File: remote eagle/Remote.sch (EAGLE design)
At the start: 17 parts, among them IC1 ATmega328p, J1 ISP Touch, Y1 16MHz, Y2 ANTENNA2ANTENNA-CHIP_1204

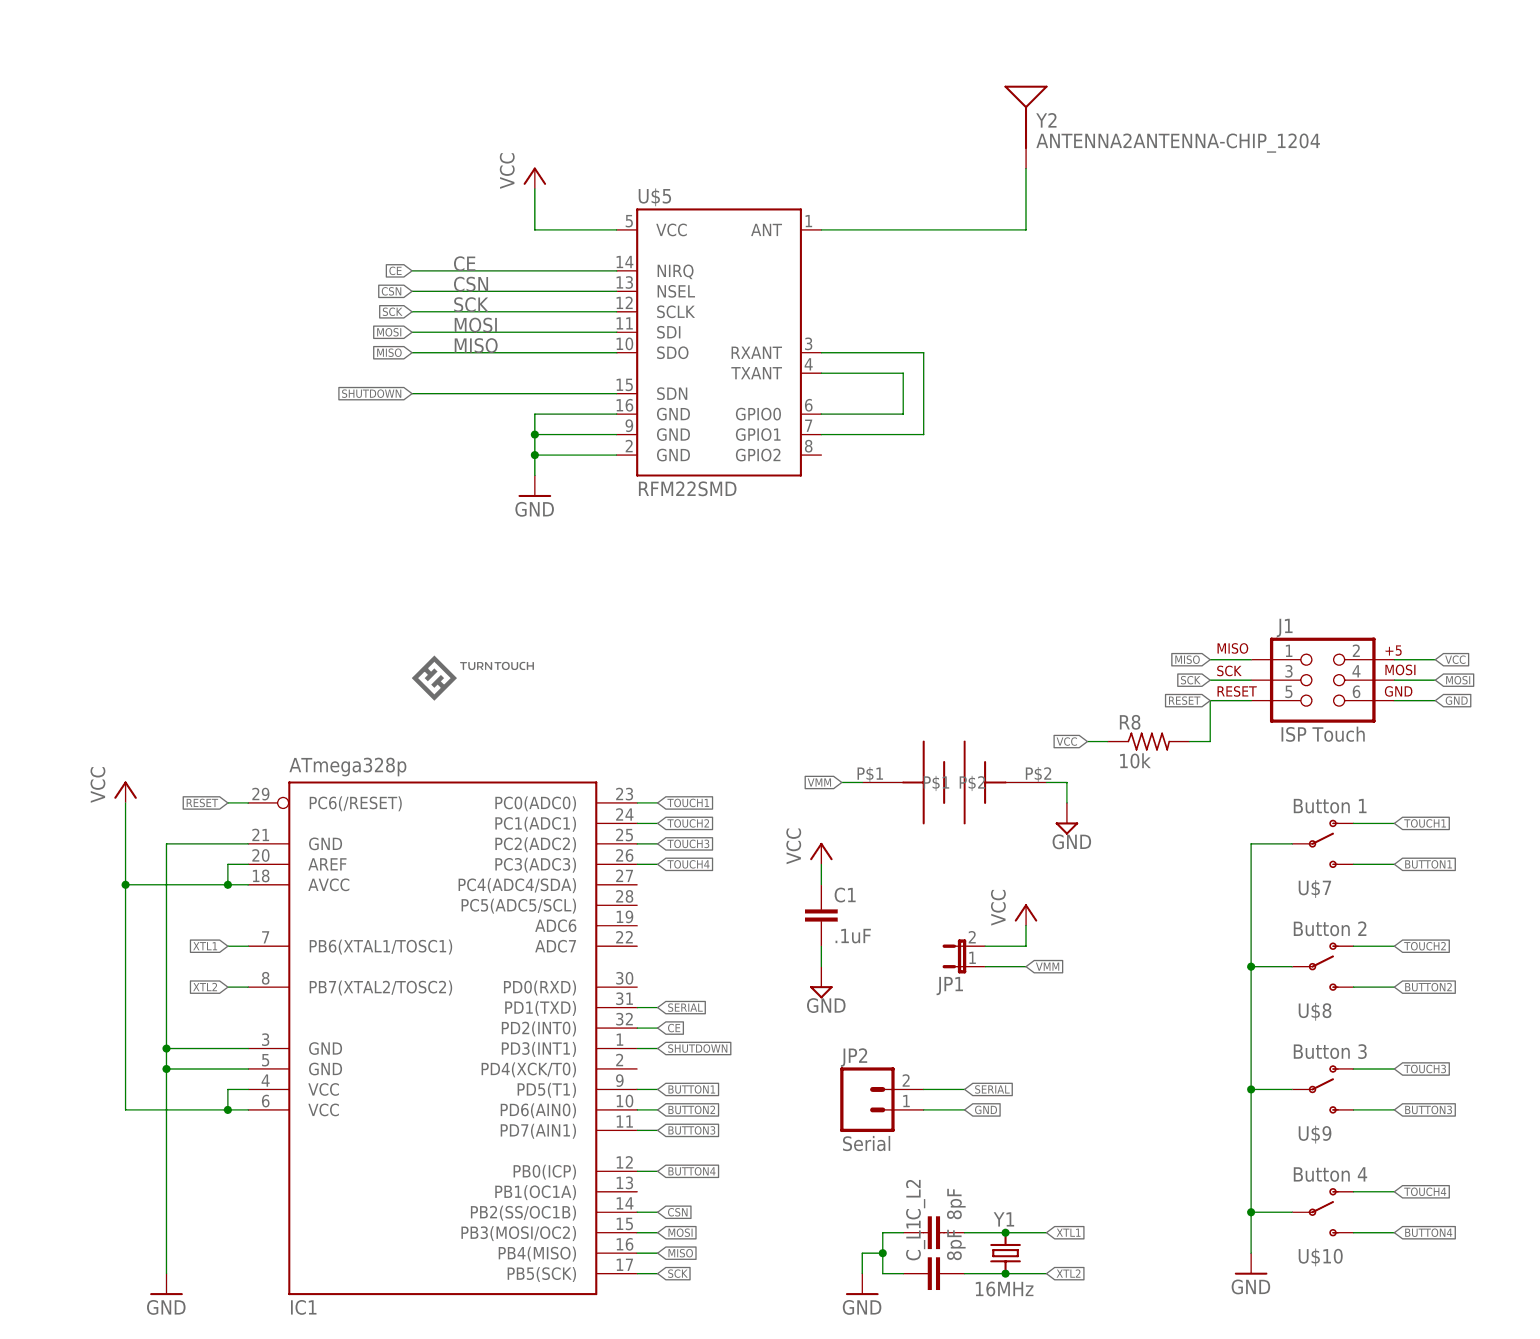
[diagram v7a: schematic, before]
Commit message: Switching to BLE112 and new P-Series dome by Snaptron in schematic and board.
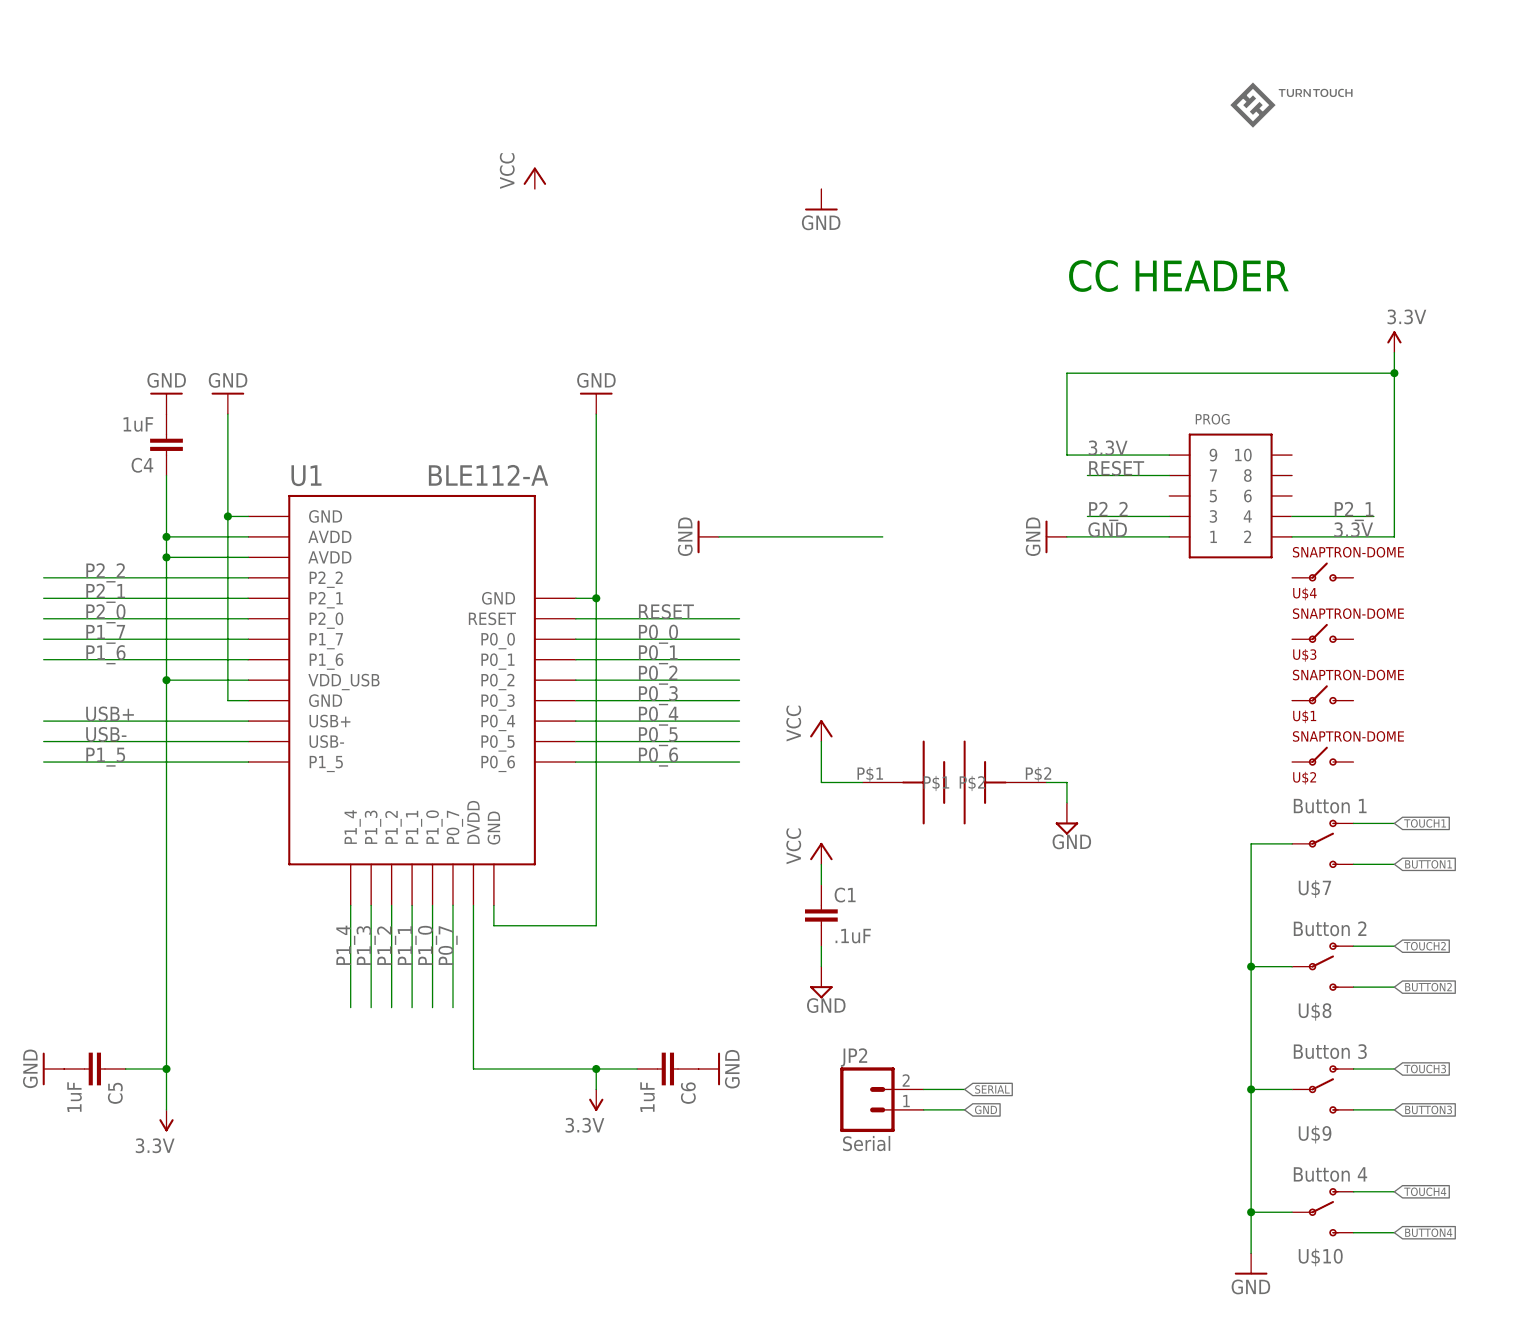
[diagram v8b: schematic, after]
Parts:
- removed C_L1, C_L2: 8pF, SparkFun-Passives:CAP0402-CAP
- removed IC1: ATmega328p, atmel:MEGA8-MI
- removed J1: ISP Touch, remote:ISPTOUCH_HEADER
- removed JP1: (no value), SparkFun-Passives:JUMPER-2SMD-NC
- removed R8: 10k, resistor:R-US_R0402
- removed U$5: RFM22SMD, remote:RFM22SMD
- removed Y1: 16MHz, remote:CRYSTAL5X3.2
- removed Y2: ANTENNA2ANTENNA-CHIP_1204, remote:ANTENNA2ANTENNA-CHIP_1204
- added C4, C5, C6: 1uF, SparkFun:CAP0603-CAP
- added PROG: CONN_5-2-FTSH-V, pel_misc:CONN_5-2-FTSH-V
- added U$1, U$2, U$3, U$4: SNAPTRON-DOME, remote:SNAPTRON-DOME
- added U1: BLE112-A, sf-bluegiga:BLE112-A-VISUAL
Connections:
- removed net CE: IC1.PD2(INT0), U$5.NIRQ
- removed net CSN: IC1.PB2(SS/OC1B), U$5.NSEL
- removed net MISO: IC1.PB4(MISO), J1.1, U$5.SDO
- removed net MOSI: IC1.PB3(MOSI/OC2), J1.4, U$5.SDI
- removed net N$2: U$5.ANT, Y2.SIGNAL
- removed net N$3: U$5.GPIO1, U$5.RXANT
- removed net N$4: U$5.GPIO0, U$5.TXANT
- removed net SCK: IC1.PB5(SCK), J1.3, U$5.SCLK
- removed net SHUTDOWN: IC1.PD3(INT1), U$5.SDN
- removed net VMM: JP1.1, U$6.P$1
- removed net XTL1: C_L2.2, IC1.PB6(XTAL1/TOSC1), Y1.2
- removed net XTL2: C_L1.2, IC1.PB7(XTAL2/TOSC2), Y1.1
- new net 3.3V: C4.1, C5.1, C6.2, PROG.2, PROG.9, U1.AVDD, U1.AVDD@2, U1.DVDD, U1.VDD_USB
- new net P0_0: U1.P0_0
- new net P0_1: U1.P0_1
- new net P0_2: U1.P0_2
- new net P0_3: U1.P0_3
- new net P0_4: U1.P0_4
- new net P0_5: U1.P0_5
- new net P0_6: U1.P0_6
- new net P0_7: U1.P0_7
- new net P1_0: U1.P1_0
- new net P1_1: U1.P1_1
- new net P1_2: U1.P1_2
- new net P1_3: U1.P1_3
- new net P1_4: U1.P1_4
- new net P1_5: U1.P1_5
- new net P1_6: U1.P1_6
- new net P1_7: U1.P1_7
- new net P2_0: U1.P2_0
- new net P2_1: PROG.4, U1.P2_1
- new net P2_2: PROG.3, U1.P2_2
- new net USB+: U1.USB+
- new net USB-: U1.USB-
- net BUTTON1: no longer IC1.PD5(T1)
- net BUTTON2: no longer IC1.PD6(AIN0)
- net BUTTON3: no longer IC1.PD7(AIN1)
- net BUTTON4: no longer IC1.PB0(ICP)
- net GND: now also C4.2, C5.2, C6.1, PROG.1, U1.GND, U1.GND@2, U1.GND@3, U1.GND@4; no longer C_L1.1, C_L2.1, IC1.GND, IC1.GND@1, IC1.GND@2, J1.6, U$5.GND@1, U$5.GND@2, U$5.GND@3
- net RESET: now also PROG.7, U1.RESET; no longer IC1.PC6(/RESET), J1.5, R8.2
- net SERIAL: no longer IC1.PD1(TXD)
- net TOUCH1: no longer IC1.PC0(ADC0)
- net TOUCH2: no longer IC1.PC1(ADC1)
- net TOUCH3: no longer IC1.PC2(ADC2)
- net TOUCH4: no longer IC1.PC3(ADC3)
- net VCC: now also U$6.P$1; no longer IC1.AREF, IC1.AVCC, IC1.VCC@1, IC1.VCC@2, J1.2, JP1.2, R8.1, U$5.VCC
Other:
- note added: "CC HEADER"
